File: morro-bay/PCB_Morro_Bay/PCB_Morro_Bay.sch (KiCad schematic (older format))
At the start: 13 parts

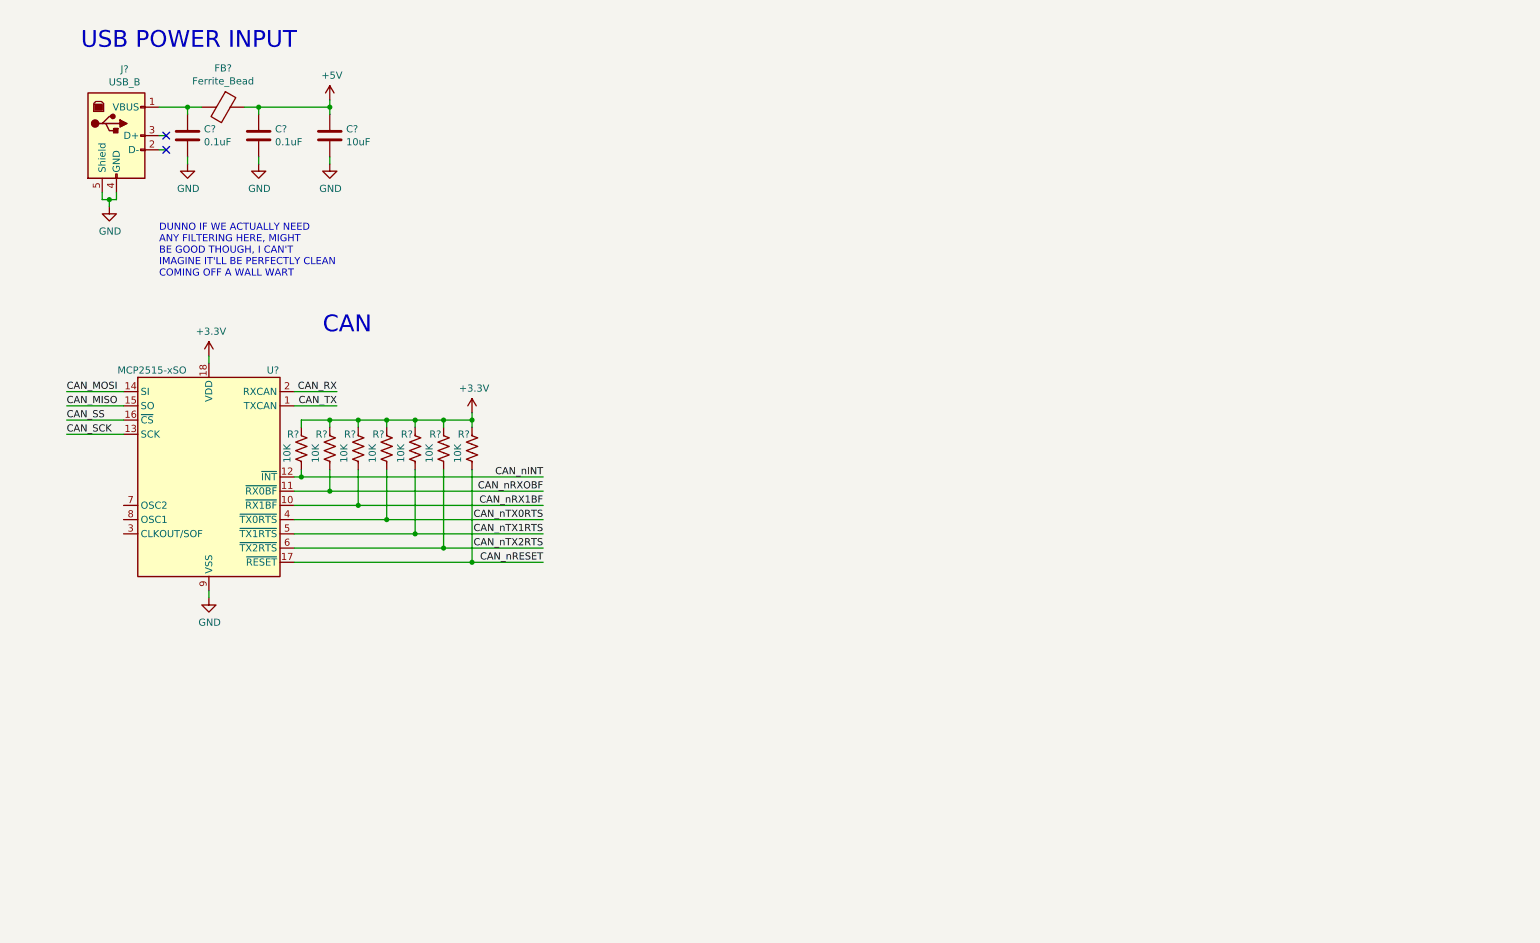
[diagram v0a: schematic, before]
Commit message: Add SAMD21, 3.3V regulator
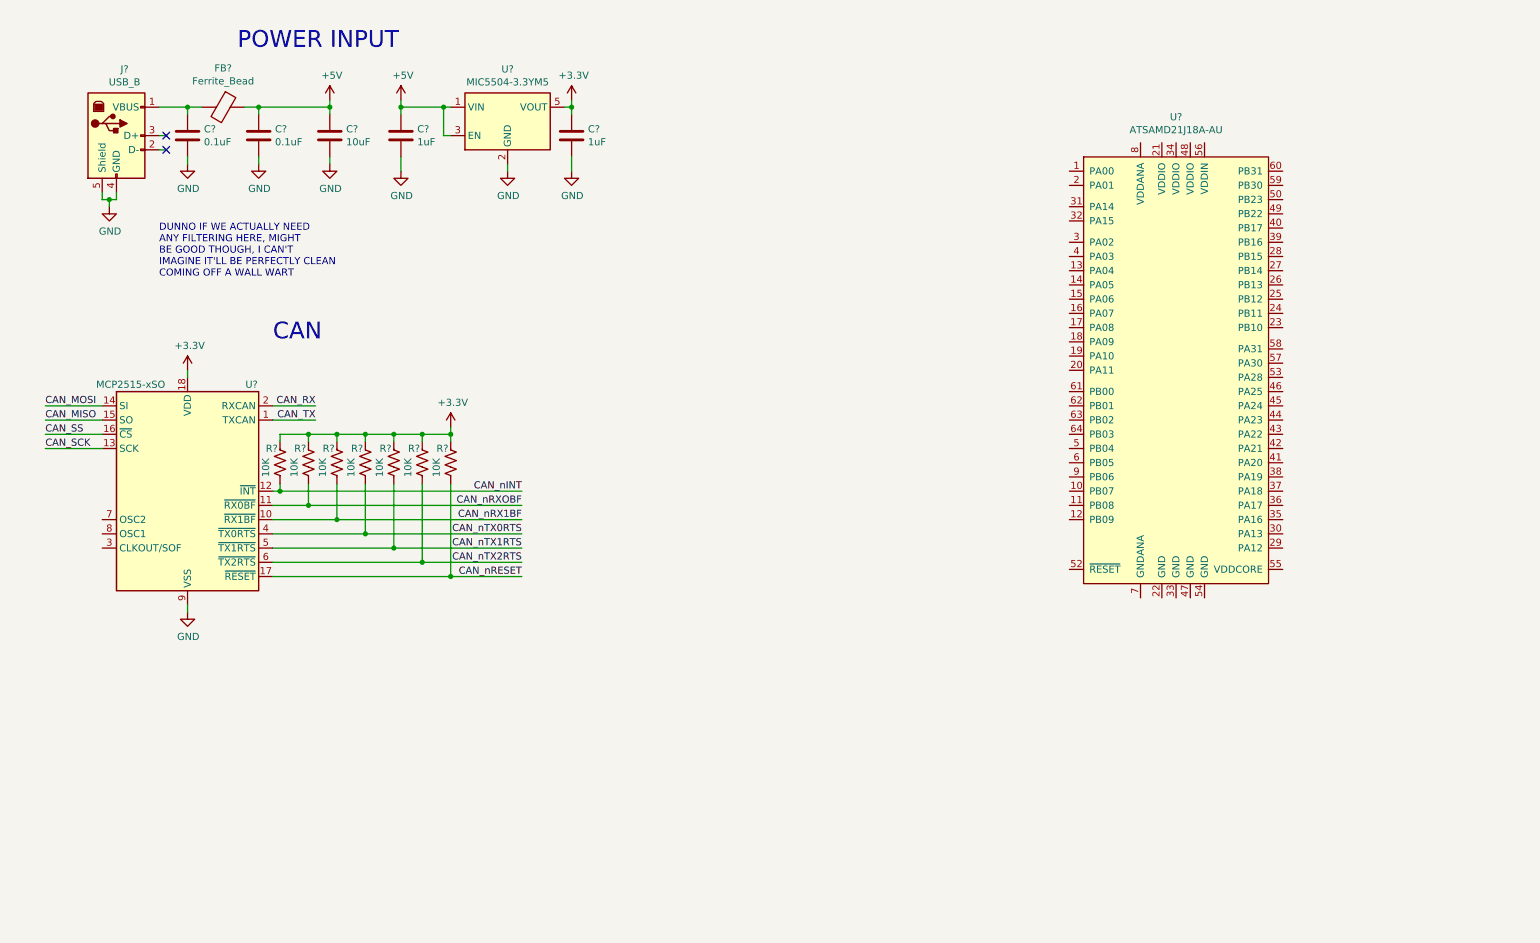
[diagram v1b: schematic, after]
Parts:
- added C? (x2): 1uF, symbol Device:C
- added U?: ATSAMD21J18A-AU, Package_QFP:TQFP-64_10x10mm_P0.5mm, symbol Morro_Bay_Lib:ATSAMD21J18A-AU
- added U?: MIC5504-3.3YM5, Package_TO_SOT_SMD:SOT-23-5, symbol Regulator_Linear:MIC5504-3.3YM5
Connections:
- net +3V3: now also C?.1, U?.5 (VOUT)
- net +5V: now also C?.1, U?.1 (VIN), U?.3 (EN)
- net GND: now also C?.2, C?.2, U?.2 (GND)
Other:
- note added: "POWER INPUT"
- note removed: "USB POWER INPUT"
- moved on the sheet: R?, U?

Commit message: Add CAN transceiver
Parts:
- added C? (x3): 0.1uF, symbol Device:C
- added J?: Conn_01x02, symbol Connector_Generic:Conn_01x02
- added R?: 120, symbol Device:R_US
- added U?: MCP2558FD-xSN, Package_SO:SOIC-8_3.9x4.9mm_P1.27mm, symbol Interface_CAN_LIN:MCP2558FD-xSN
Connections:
- net labels added: CANH, CANL, CAN_SILENT, CAN_TERM, V_UNFILT
- wire segments 73 -> 91
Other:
- moved on the sheet: U?
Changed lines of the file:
@@
 L Morro_Bay_Lib:ATSAMD21J18A-AU U?
 U 1 1 5E3C105D
-P 8750 3050
-F 0 "U?" H 8750 4831 50  0000 C CNN
-F 1 "ATSAMD21J18A-AU" H 8750 4740 50  0000 C CNN
-F 2 "Package_QFP:TQFP-64_10x10mm_P0.5mm" H 8900 3750 50  0001 C CNN
-F 3 "http://ww1.microchip.com/downloads/en/DeviceDoc/SAM_D21_DA1_Family_Data%20Sheet_DS40001882E.pdf" H 8900 3750 50  0001 C CNN
-	1    8750 3050
+P 9700 2950
+F 0 "U?" H 9700 2950 50  0000 C CNN
+F 1 "ATSAMD21J18A-AU" H 9700 3050 50  0000 C CNN
+F 2 "Package_QFP:TQFP-64_10x10mm_P0.5mm" H 9850 3650 50  0001 C CNN
+F 3 "http://ww1.microchip.com/downloads/en/DeviceDoc/SAM_D21_DA1_Family_Data%20Sheet_DS40001882E.pdf" H 9850 3650 50  0001 C CNN
+	1    9700 2950
 	1    0    0    -1
 $EndComp
@@
 	4500 1250 4500 1200
 Connection ~ 4500 1200
+$Comp
+L Interface_CAN_LIN:MCP2558FD-xSN U?
+U 1 1 5E3E9C24
+P 5250 3500
+F 0 "U?" H 5600 3850 50  0000 C CNN
+F 1 "MCP2558FD-xSN" H 4800 3850 50  0000 C CNN
+F 2 "Package_SO:SOIC-8_3.9x4.9mm_P1.27mm" H 5250 2900 50  0001 C CNN
+F 3 "https://ww1.microchip.com/downloads/en/DeviceDoc/20005533A.pdf" H 5250 3500 50  0001 C CNN
+	1    5250 3500
+	1    0    0    -1
+$EndComp
+$Comp
+L power:+3.3V #PWR?
+U 1 1 5E3EAEA7
+P 1300 5000
+F 0 "#PWR?" H 1300 4850 50  0001 C CNN
+F 1 "+3.3V" H 1315 5173 50  0000 C CNN
+F 2 "" H 1300 5000 50  0001 C CNN
+F 3 "" H 1300 5000 50  0001 C CNN
+	1    1300 5000
+	1    0    0    -1
+$EndComp
+$Comp
+L power:GND #PWR?
+U 1 1 5E3EB860
+P 1300 5400
+F 0 "#PWR?" H 1300 5150 50  0001 C CNN
+F 1 "GND" H 1305 5227 50  0000 C CNN
+F 2 "" H 1300 5400 50  0001 C CNN
+F 3 "" H 1300 5400 50  0001 C CNN
+	1    1300 5400
+	1    0    0    -1
+$EndComp
+$Comp
+L Device:C C?
+U 1 1 5E3EBD32
+P 1300 5200
+F 0 "C?" H 1415 5246 50  0000 L CNN
+F 1 "0.1uF" H 1415 5155 50  0000 L CNN
+F 2 "" H 1338 5050 50  0001 C CNN
+F 3 "~" H 1300 5200 50  0001 C CNN
+	1    1300 5200
+	1    0    0    -1
+$EndComp
+Wire Wire Line
+	1300 5000 1300 5050
+Wire Wire Line
+	1300 5350 1300 5400
+Text Label 4450 3400 0    50   ~ 0
+CAN_RX
+Wire Wire Line
+	4450 3400 4750 3400
+Wire Wire Line
+	4750 3300 4450 3300
+Text Label 4450 3300 0    50   ~ 0
+CAN_TX
+$Comp
+L power:+5V #PWR?
+U 1 1 5E3F665B
+P 5250 3050
+F 0 "#PWR?" H 5250 2900 50  0001 C CNN
+F 1 "+5V" H 5265 3223 50  0000 C CNN
+F 2 "" H 5250 3050 50  0001 C CNN
+F 3 "" H 5250 3050 50  0001 C CNN
+	1    5250 3050
+	1    0    0    -1
+$EndComp
+Wire Wire Line
+	5250 3050 5250 3100
+$Comp
+L power:GND #PWR?
+U 1 1 5E3F89BA
+P 5250 3950
+F 0 "#PWR?" H 5250 3700 50  0001 C CNN
+F 1 "GND" H 5255 3777 50  0000 C CNN
+F 2 "" H 5250 3950 50  0001 C CNN
+F 3 "" H 5250 3950 50  0001 C CNN
+	1    5250 3950
+	1    0    0    -1
+$EndComp
+Wire Wire Line
+	5250 3900 5250 3950
+Wire Wire Line
+	4750 3600 4300 3600
+Wire Wire Line
+	4300 3600 4300 3550
+$Comp
+L power:+3.3V #PWR?
+U 1 1 5E3FCAAC
+P 4300 3550
+F 0 "#PWR?" H 4300 3400 50  0001 C CNN
+F 1 "+3.3V" H 4315 3723 50  0000 C CNN
+F 2 "" H 4300 3550 50  0001 C CNN
+F 3 "" H 4300 3550 50  0001 C CNN
+	1    4300 3550
+	1    0    0    -1
+$EndComp
+Wire Wire Line
+	5750 3400 5950 3400
+Wire Wire Line
+	5750 3600 5950 3600
+Text Label 5950 3400 2    50   ~ 0
+CANH
+Text Label 5950 3600 2    50   ~ 0
+CANL
+Text Label 4300 3700 0    50   ~ 0
+CAN_SILENT
+Wire Wire Line
+	4300 3700 4750 3700
+$Comp
+L power:+3.3V #PWR?
+U 1 1 5E408C46
+P 5000 4400
+F 0 "#PWR?" H 5000 4250 50  0001 C CNN
+F 1 "+3.3V" H 5015 4573 50  0000 C CNN
+F 2 "" H 5000 4400 50  0001 C CNN
+F 3 "" H 5000 4400 50  0001 C CNN
+	1    5000 4400
+	1    0    0    -1
+$EndComp
+$Comp
+L power:GND #PWR?
+U 1 1 5E408C50
+P 5000 4800
+F 0 "#PWR?" H 5000 4550 50  0001 C CNN
+F 1 "GND" H 5005 4627 50  0000 C CNN
+F 2 "" H 5000 4800 50  0001 C CNN
+F 3 "" H 5000 4800 50  0001 C CNN
+	1    5000 4800
+	1    0    0    -1
+$EndComp
+$Comp
+L Device:C C?
+U 1 1 5E408C5A
+P 5000 4600
+F 0 "C?" H 5115 4646 50  0000 L CNN
+F 1 "0.1uF" H 5115 4555 50  0000 L CNN
+F 2 "" H 5038 4450 50  0001 C CNN
+F 3 "~" H 5000 4600 50  0001 C CNN
+	1    5000 4600
+	1    0    0    -1
+$EndComp
+Wire Wire Line
+	5000 4400 5000 4450
+Wire Wire Line
+	5000 4750 5000 4800
+$Comp
+L power:GND #PWR?
+U 1 1 5E40CE6D
+P 5450 4800
+F 0 "#PWR?" H 5450 4550 50  0001 C CNN
+F 1 "GND" H 5455 4627 50  0000 C CNN
+F 2 "" H 5450 4800 50  0001 C CNN
+F 3 "" H 5450 4800 50  0001 C CNN
+	1    5450 4800
+	1    0    0    -1
+$EndComp
+$Comp
+L Device:C C?
+U 1 1 5E40CE77
+P 5450 4600
+F 0 "C?" H 5565 4646 50  0000 L CNN
+F 1 "0.1uF" H 5565 4555 50  0000 L CNN
+F 2 "" H 5488 4450 50  0001 C CNN
+F 3 "~" H 5450 4600 50  0001 C CNN
+	1    5450 4600
+	1    0    0    -1
+$EndComp
+Wire Wire Line
+	5450 4400 5450 4450
+Wire Wire Line
+	5450 4750 5450 4800
+$Comp
+L power:+5V #PWR?
+U 1 1 5E4100D6
+P 5450 4400
+F 0 "#PWR?" H 5450 4250 50  0001 C CNN
+F 1 "+5V" H 5465 4573 50  0000 C CNN
+F 2 "" H 5450 4400 50  0001 C CNN
+F 3 "" H 5450 4400 50  0001 C CNN
+	1    5450 4400
+	1    0    0    -1
+$EndComp
+Text Label 2650 5000 0    50   ~ 0
+CANH
+$Comp
+L Connector_Generic:Conn_01x02 J?
+U 1 1 5E4145BC
+P 3450 5000
+F 0 "J?" H 3530 4992 50  0000 L CNN
+F 1 "Conn_01x02" H 3530 4901 50  0000 L CNN
+F 2 "" H 3450 5000 50  0001 C CNN
+F 3 "~" H 3450 5000 50  0001 C CNN
+	1    3450 5000
+	1    0    0    -1
+$EndComp
+Wire Wire Line
+	2650 5000 3250 5000
+Text Label 2650 5100 0    50   ~ 0
+CANL
+Wire Wire Line
+	3150 5100 3250 5100
+Wire Wire Line
+	2650 5100 2850 5100
+$Comp
+L Device:R_US R?
+U 1 1 5E42C915
+P 3000 5100
+F 0 "R?" V 3200 5100 50  0000 C CNN
+F 1 "120" V 3100 5100 50  0000 C CNN
+F 2 "" V 3040 5090 50  0001 C CNN
+F 3 "~" H 3000 5100 50  0001 C CNN
+	1    3000 5100
+	0    1    1    0
+$EndComp
+Text Label 3200 5100 3    50   ~ 0
+CAN_TERM
+Text Label 1600 1200 0    50   ~ 0
+V_UNFILT
 $EndSCHEMATC

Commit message: Change CAN transceiver to 3.3V
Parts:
- removed C?: 0.1uF, symbol Device:C
- removed U?: MCP2558FD-xSN, Package_SO:SOIC-8_3.9x4.9mm_P1.27mm, symbol Interface_CAN_LIN:MCP2558FD-xSN
- added U3: SN65HVD232, Package_SO:SOIC-8_3.9x4.9mm_P1.27mm, symbol Interface_CAN_LIN:SN65HVD232
- gave numbers to parts that had none: 21
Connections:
- net labels removed: CAN_SILENT
- wire segments 91 -> 86
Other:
- moved on the sheet: C7

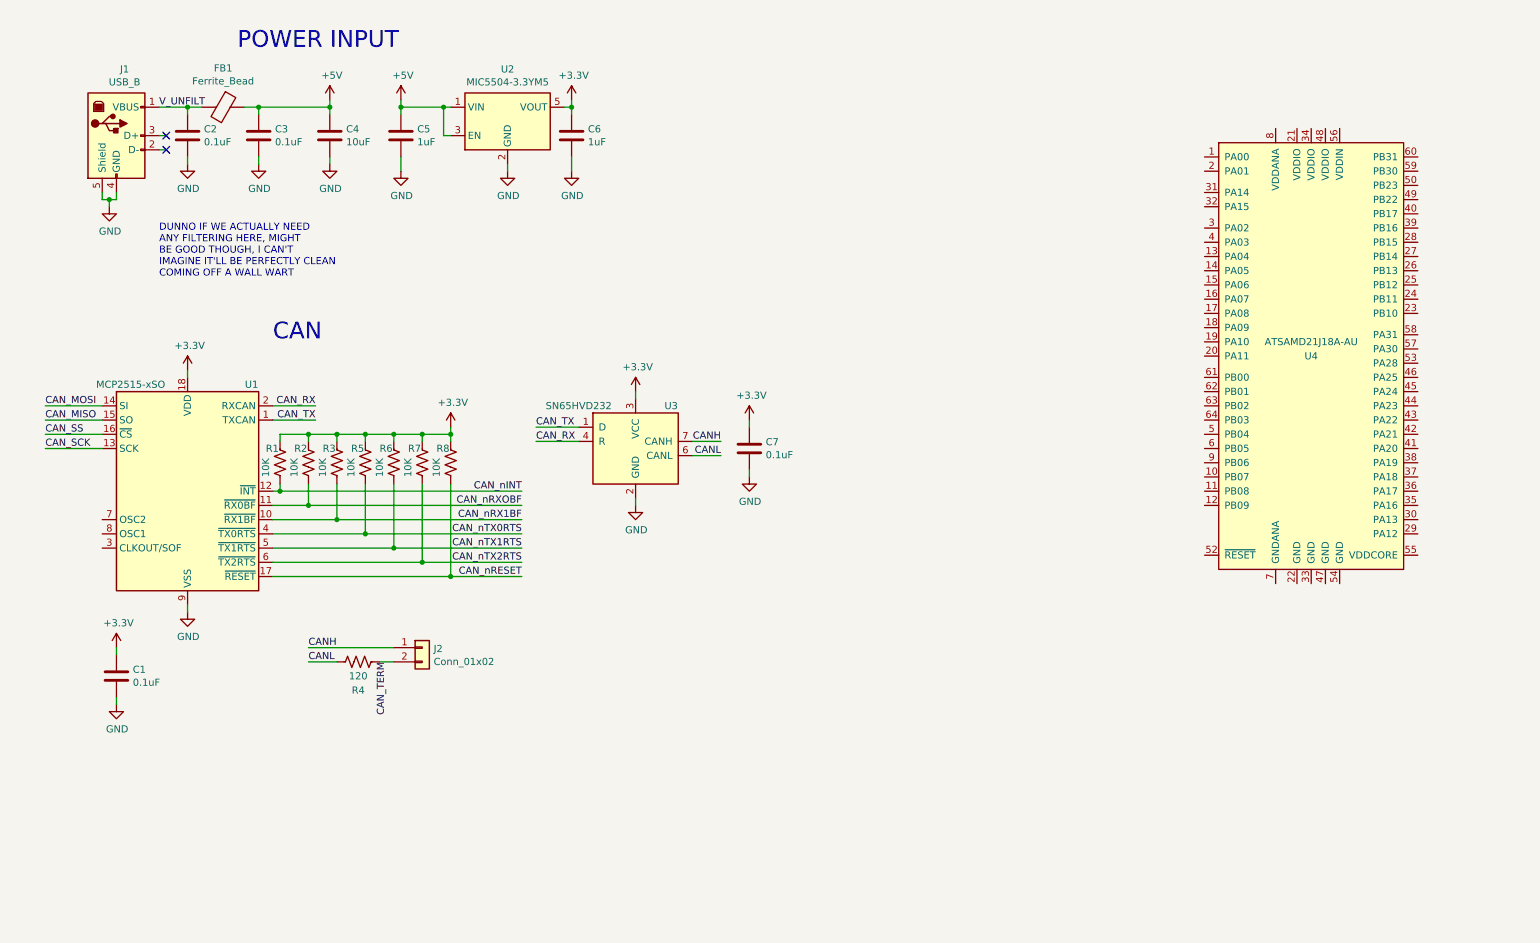
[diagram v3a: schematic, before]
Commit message: Add decoupling and analog power filtering for SAMD
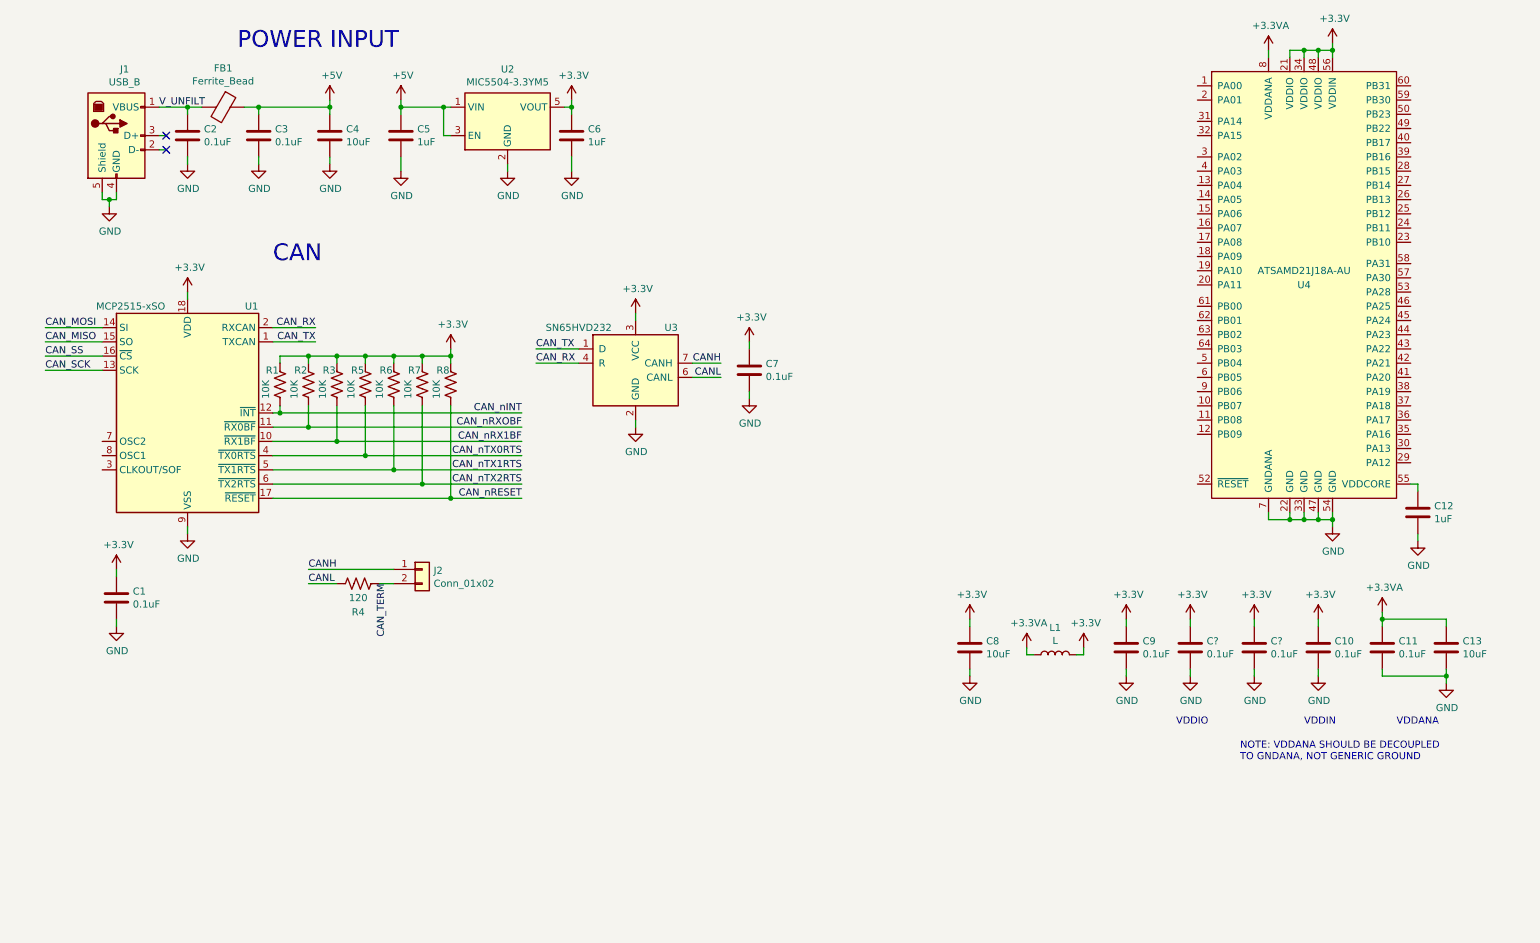
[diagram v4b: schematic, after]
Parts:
- added C10, C11, C9, C? (x2): 0.1uF, symbol Device:C
- added C12: 1uF, symbol Device:C
- added C13, C8: 10uF, symbol Device:C
- added L1: L, symbol Device:L
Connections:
- net +3V3: now also U4.21 (VDDIO), U4.34 (VDDIO), U4.48 (VDDIO), U4.56 (VDDIN), C10.1, C8.1, C9.1, C?.1, C?.1, L1.2
- net GND: now also U4.22 (GND), U4.33 (GND), U4.47 (GND), U4.54 (GND), U4.7 (GNDANA), C10.2, C11.2, C12.2, C13.2, C8.2, C9.2, C?.2, C?.2
- net at U4.55 (VDDCORE): now also C12.1
- net +3.3VA: now reaches U4.8 (VDDANA)
- net +3.3VA: now also C11.1, C13.1, L1.1
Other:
- note added: "NOTE: VDDANA SHOULD BE DECOUPLED\nTO GNDANA, NOT GENERIC GROUND"
- note added: "VDDANA"
- note added: "VDDIN"
- note added: "VDDIO"
- note removed: "DUNNO IF WE ACTUALLY NEED\nANY FILTERING HERE, MIGHT\nBE GOOD THOUGH, I CAN'T\nIMAGINE IT'LL BE PERFECTLY CLEAN\nCOMING OFF A WALL WART"
- moved on the sheet: C1, C7, J2, R1, R2, R3, R4, R5, R6, R7, R8, U1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
